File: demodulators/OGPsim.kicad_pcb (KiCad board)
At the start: 4 copper layers, 29.5 x 9.7 mm, 36 parts, among them U2 AD8668ARZ-ND

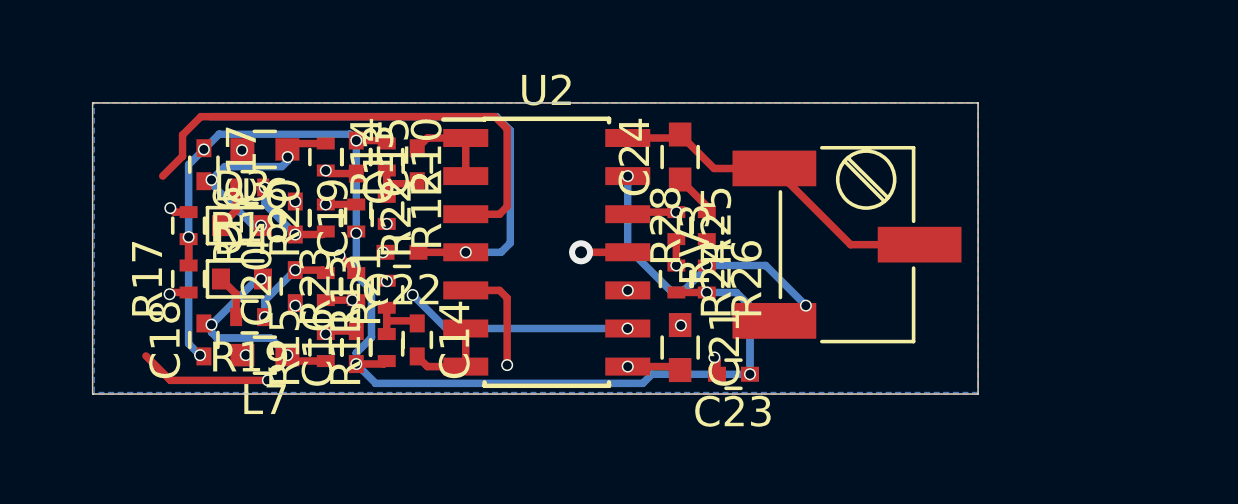
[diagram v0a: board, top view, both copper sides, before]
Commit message: Removed 1 ohm resistors as it was only used for simulating parasitic resistance in tank circuit.
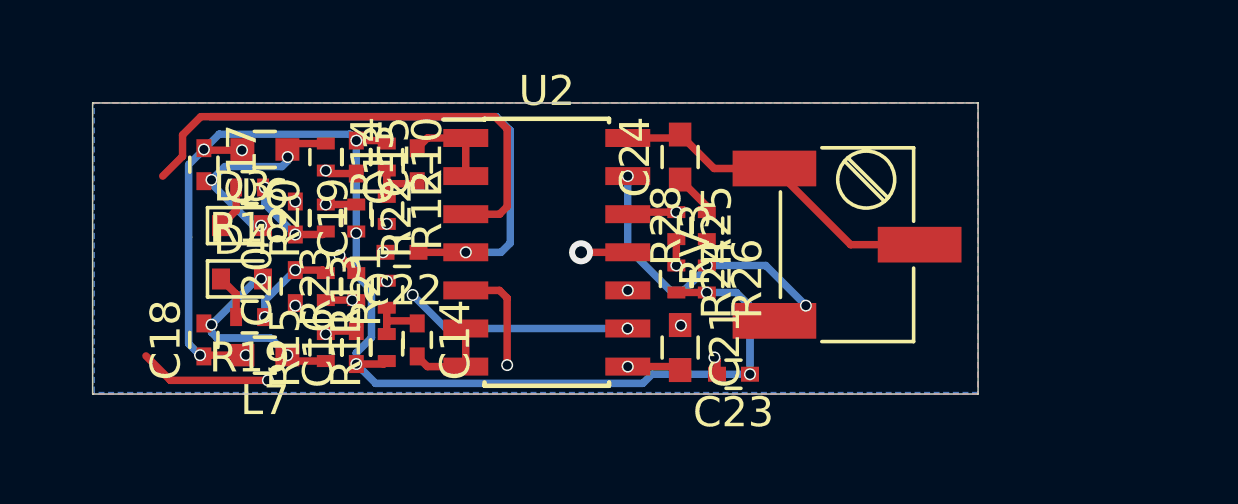
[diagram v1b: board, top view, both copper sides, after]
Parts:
- removed R16, R17: 1ohm, Resistors_SMD:R_0402
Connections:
- C19 pad 1: Net-(C19-Pad1) -> +4V
- C20 pad 1: Net-(C20-Pad1) -> +4V
- L6 pad 2: Net-(C19-Pad1) -> +4V
- L7 pad 2: Net-(C20-Pad1) -> +4V
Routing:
- net Net-(C20-Pad1): track 8.52 -> 0.00 mm, vias 3 -> 0
- net Net-(C19-Pad1): track 8.17 -> 0.00 mm, vias 3 -> 0
- net +4V: track 42.0 -> 49.2 mm, vias 8 -> 11

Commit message: Added Solder Pads To Demodulator Board
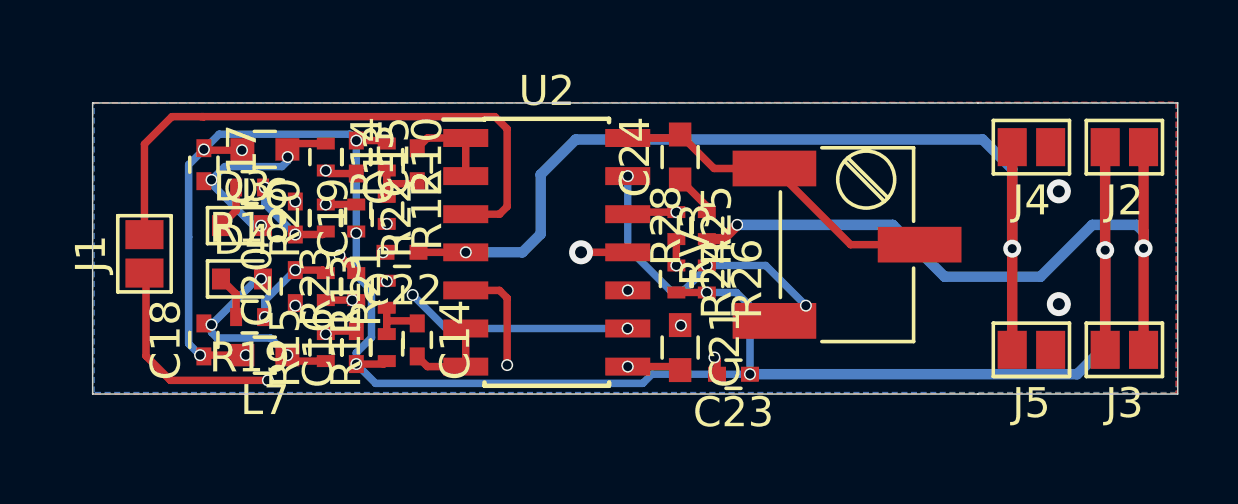
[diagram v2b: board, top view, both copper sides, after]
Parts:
- added J1: Conn_01x02, Connect:GS2, F.Cu at (133.1, 102.3)
- added J2: Conn_01x02, Connect:GS2, F.Cu at (165.8, 98.7)
- added J3: Conn_01x02, Connect:GS2, F.Cu at (165.8, 105.5)
- added J4: Conn_01x02, Connect:GS2, F.Cu at (162.7, 98.7)
- added J5: Conn_01x02, Connect:GS2, F.Cu at (162.7, 105.5)
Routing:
- net Net-(J2-Pad1): track 0.00 -> 23.6 mm, vias 0 -> 2
- net +4V: track 49.2 -> 71.5 mm, vias 11 -> 12
- net +9V: track 17.1 -> 32.3 mm, vias 1 -> 2
- net Net-(J1-Pad2): track 17.0 -> 19.8 mm
- net Net-(J1-Pad1): track 16.3 -> 19.1 mm
- net GND: vias 2 -> 4
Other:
- board size 29.5 x 9.7 mm -> 36.2 x 9.7 mm

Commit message: Added solder pads to pickup and adjusted placement of solder pads on demodulator.
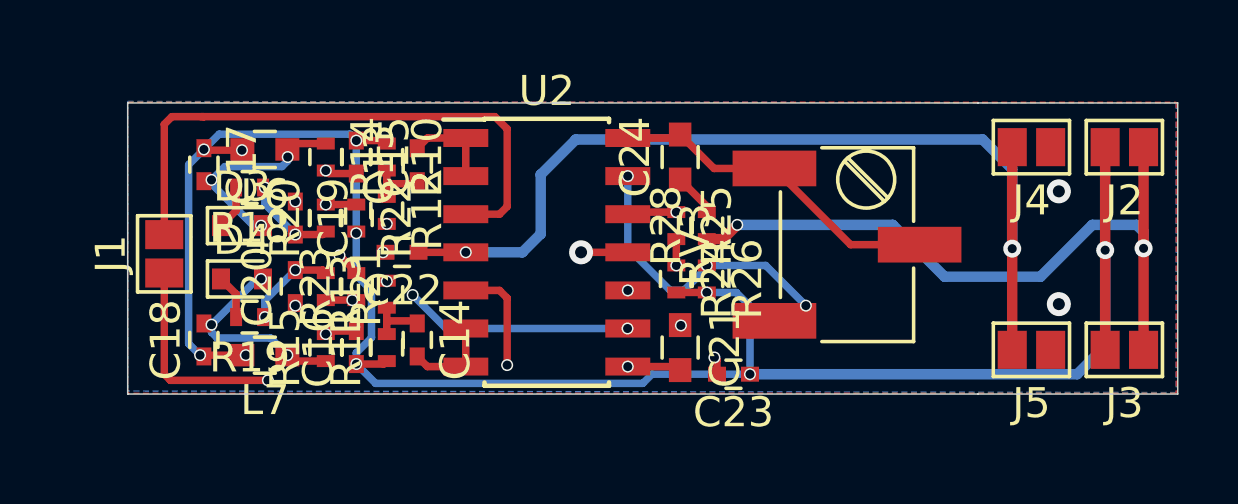
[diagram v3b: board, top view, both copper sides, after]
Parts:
- moved J1 0.66 mm to (133.8, 102.3)
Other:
- board size 36.2 x 9.7 mm -> 35 x 9.7 mm

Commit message: Cleaned up silk screen layers and moved part REFs to UserDrawings. Made PNG image file of part REFs for Power Supply and Pickup Boards.
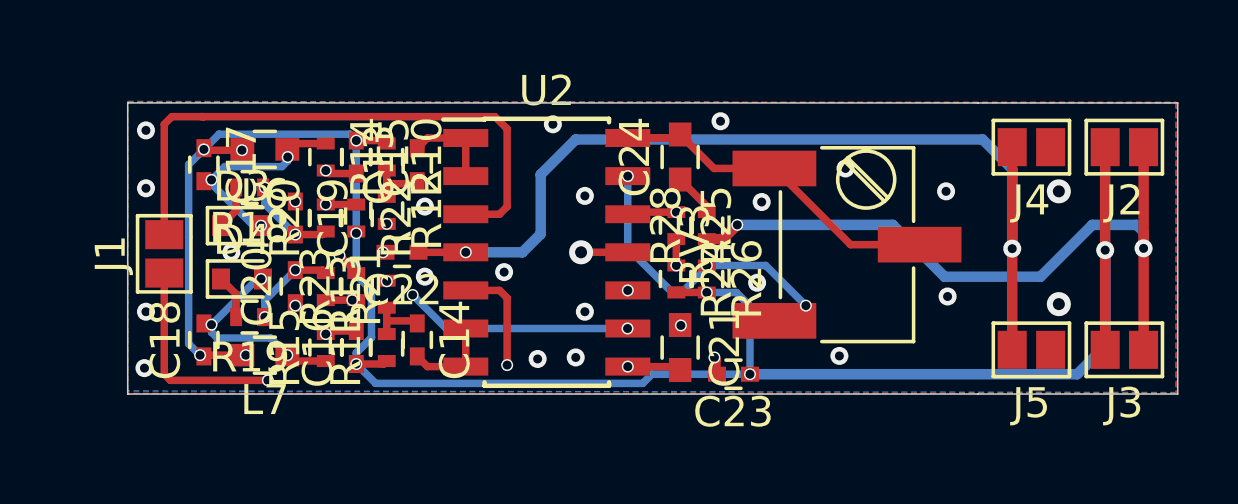
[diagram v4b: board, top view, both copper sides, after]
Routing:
- net GND: vias 4 -> 24
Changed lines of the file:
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@@
     (thickness 1.6)
     (drawings 8)
-    (tracks 269)
+    (tracks 289)
     (zones 0)
     (modules 39)
@@
     (35 F.Paste user)
     (36 B.SilkS user)
-    (37 F.SilkS user hide)
+    (37 F.SilkS user)
     (38 B.Mask user)
     (39 F.Mask user)
@@
   )
   (dimension 9.7028 (width 0.15) (layer Dwgs.User)
-    (gr_text "9.703 mm" (at 128.0368 102.0826 90) (layer Dwgs.User)
-      (effects (font (size 1 1) (thickness 0.15)))
-    )
-    (feature1 (pts (xy 131.8768 97.2312) (xy 128.750379 97.2312)))
-    (feature2 (pts (xy 131.8768 106.934) (xy 128.750379 106.934)))
-    (crossbar (pts (xy 129.3368 106.934) (xy 129.3368 97.2312)))
-    (arrow1a (pts (xy 129.3368 97.2312) (xy 129.923221 98.357704)))
-    (arrow1b (pts (xy 129.3368 97.2312) (xy 128.750379 98.357704)))
-    (arrow2a (pts (xy 129.3368 106.934) (xy 129.923221 105.807496)))
-    (arrow2b (pts (xy 129.3368 106.934) (xy 128.750379 105.807496)))
+    (gr_text "9.703 mm" (at 128.0368 101.89464 90) (layer Dwgs.User)
+      (effects (font (size 1 1) (thickness 0.15)))
+    )
+    (feature1 (pts (xy 131.8768 97.04324) (xy 128.750379 97.04324)))
+    (feature2 (pts (xy 131.8768 106.74604) (xy 128.750379 106.74604)))
+    (crossbar (pts (xy 129.3368 106.74604) (xy 129.3368 97.04324)))
+    (arrow1a (pts (xy 129.3368 97.04324) (xy 129.923221 98.169744)))
+    (arrow1b (pts (xy 129.3368 97.04324) (xy 128.750379 98.169744)))
+    (arrow2a (pts (xy 129.3368 106.74604) (xy 129.923221 105.619536)))
+    (arrow2b (pts (xy 129.3368 106.74604) (xy 128.750379 105.619536)))
   )
   (dimension 35.0012 (width 0.15) (layer Dwgs.User)
-    (gr_text "35.001 mm" (at 150.0378 112.044) (layer Dwgs.User)
-      (effects (font (size 1 1) (thickness 0.15)))
-    )
-    (feature1 (pts (xy 132.5372 108.5596) (xy 132.5372 111.330421)))
-    (feature2 (pts (xy 167.5384 108.5596) (xy 167.5384 111.330421)))
-    (crossbar (pts (xy 167.5384 110.744) (xy 132.5372 110.744)))
-    (arrow1a (pts (xy 132.5372 110.744) (xy 133.663704 110.157579)))
-    (arrow1b (pts (xy 132.5372 110.744) (xy 133.663704 111.330421)))
-    (arrow2a (pts (xy 167.5384 110.744) (xy 166.411896 110.157579)))
-    (arrow2b (pts (xy 167.5384 110.744) (xy 166.411896 111.330421)))
+    (gr_text "35.001 mm" (at 150.0378 111.85604) (layer Dwgs.User)
+      (effects (font (size 1 1) (thickness 0.15)))
+    )
+    (feature1 (pts (xy 132.5372 108.37164) (xy 132.5372 111.142461)))
+    (feature2 (pts (xy 167.5384 108.37164) (xy 167.5384 111.142461)))
+    (crossbar (pts (xy 167.5384 110.55604) (xy 132.5372 110.55604)))
+    (arrow1a (pts (xy 132.5372 110.55604) (xy 133.663704 109.969619)))
+    (arrow1b (pts (xy 132.5372 110.55604) (xy 133.663704 111.142461)))
+    (arrow2a (pts (xy 167.5384 110.55604) (xy 166.411896 109.969619)))
+    (arrow2b (pts (xy 167.5384 110.55604) (xy 166.411896 111.142461)))
   )
   (gr_line (start 167.5384 106.934) (end 160.8836 106.934) (layer Edge.Cuts) (width 0.05))
@@
   (via (at 163.576 100.1776) (size 0.8) (drill 0.4) (layers F.Cu B.Cu) (net 1))
   (via (at 163.576 103.9368) (size 0.8) (drill 0.4) (layers F.Cu B.Cu) (net 1))
+  (via (at 159.8168 100.1776) (size 0.6) (drill 0.3) (layers F.Cu B.Cu) (net 1))
+  (via (at 159.8676 103.6828) (size 0.6) (drill 0.3) (layers F.Cu B.Cu) (net 1))
+  (via (at 156.2608 105.664) (size 0.6) (drill 0.3) (layers F.Cu B.Cu) (net 1))
+  (via (at 156.464 99.4156) (size 0.6) (drill 0.3) (layers F.Cu B.Cu) (net 1))
+  (via (at 145.0848 102.87) (size 0.6) (drill 0.3) (layers F.Cu B.Cu) (net 1))
+  (via (at 147.7772 100.33) (size 0.6) (drill 0.3) (layers F.Cu B.Cu) (net 1))
+  (via (at 147.7772 104.1908) (size 0.6) (drill 0.3) (layers F.Cu B.Cu) (net 1))
+  (via (at 147.4724 105.7148) (size 0.6) (drill 0.3) (layers F.Cu B.Cu) (net 1))
+  (via (at 146.2024 105.7656) (size 0.6) (drill 0.3) (layers F.Cu B.Cu) (net 1))
+  (via (at 142.4432 100.6856) (size 0.6) (drill 0.3) (layers F.Cu B.Cu) (net 1))
+  (via (at 142.4432 103.0224) (size 0.6) (drill 0.3) (layers F.Cu B.Cu) (net 1))
+  (via (at 133.1468 104.1908) (size 0.6) (drill 0.3) (layers F.Cu B.Cu) (net 1))
+  (via (at 133.096 106.0704) (size 0.6) (drill 0.3) (layers F.Cu B.Cu) (net 1))
+  (via (at 133.1468 98.1456) (size 0.6) (drill 0.3) (layers F.Cu B.Cu) (net 1))
+  (via (at 133.1468 100.076) (size 0.6) (drill 0.3) (layers F.Cu B.Cu) (net 1))
+  (via (at 146.7104 97.9424) (size 0.6) (drill 0.3) (layers F.Cu B.Cu) (net 1))
+  (via (at 152.2984 97.8408) (size 0.6) (drill 0.3) (layers F.Cu B.Cu) (net 1))
+  (via (at 135.9916 102.2096) (size 0.6) (drill 0.3) (layers F.Cu B.Cu) (net 1))
+  (via (at 153.67 100.5332) (size 0.6) (drill 0.3) (layers F.Cu B.Cu) (net 1))
+  (via (at 153.5176 103.2256) (size 0.6) (drill 0.3) (layers F.Cu B.Cu) (net 1))
   (via (at 143.8072 102.2096) (size 0.4) (drill 0.3) (layers F.Cu B.Cu) (net 2) (status 30))
   (segment (start 143.8072 102.2096) (end 142.2312 102.2096) (width 0.25) (layer F.Cu) (net 2) (status 30))
